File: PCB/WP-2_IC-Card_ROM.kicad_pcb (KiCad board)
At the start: 2 copper layers, 54 x 54 mm, 15 parts, among them J1 SMS-138-01-G-S, SW1 CUS-12TB, SW2 CUS-12TB, U1 29F0x0_TSOP

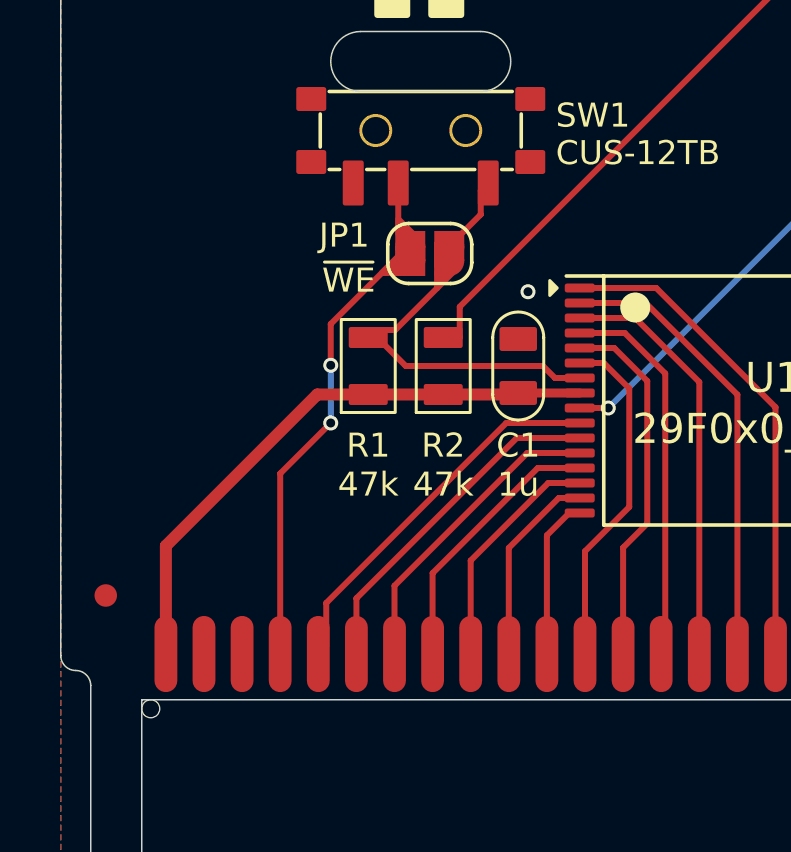
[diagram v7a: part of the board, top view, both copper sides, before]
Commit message: ROM add S3-RW hack support
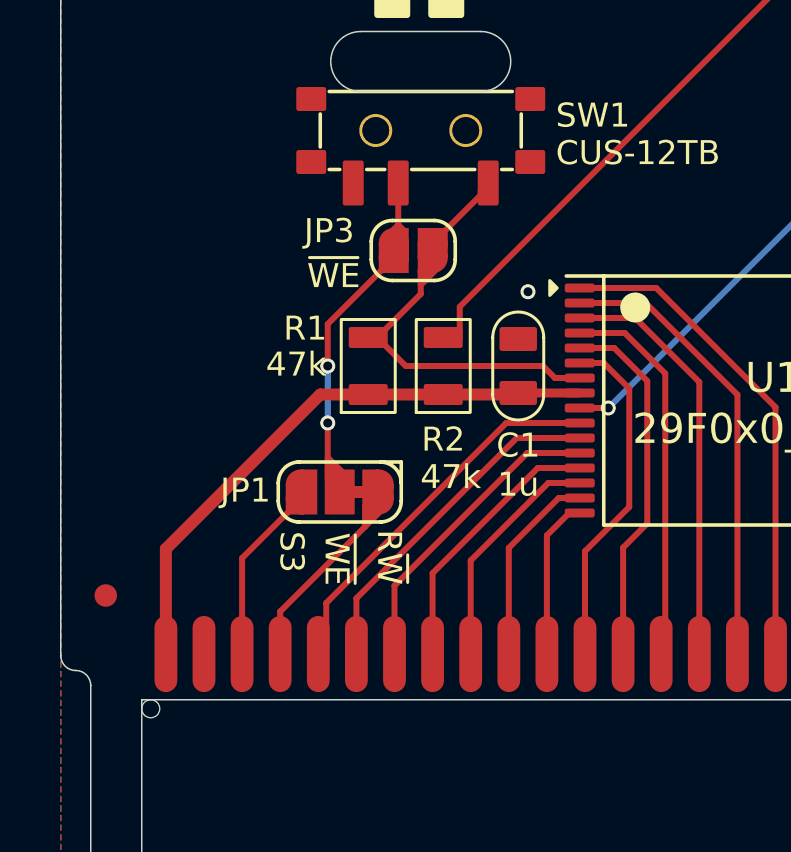
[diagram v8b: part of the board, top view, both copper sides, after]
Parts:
- added JP3: ~{WE}, 000_LOCAL:SolderJumper-2_Open, F.Cu at (120.6, 103.2)
- JP1: footprint 000_LOCAL:SolderJumper-2_open -> 000_LOCAL:SolderJumper-3_Bridged12
- moved JP1 8.50 mm to (118.2, 111.2), turned to 180 degrees
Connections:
- JP1 pad 2: /~{WE} -> Net-(JP1-C)
- SW1 pad 2: /R~{W} -> Net-(JP1-C)
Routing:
- net Net-(JP1-C): track 0.00 -> 11.4 mm, vias 0 -> 2
- net /R~{W}: track 17.3 -> 6.76 mm, vias 2 -> 0
- net /S3: track 0.00 -> 6.21 mm
